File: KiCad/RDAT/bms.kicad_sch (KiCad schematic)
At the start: 0 parts

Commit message: kiCad BMS sadness
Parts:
- added C15: C, symbol Device:C
- added C16, C17, C18, C19: 0.1uF, symbol Device:C
- added J4: Conn_01x05_MountingPin, symbol Connector_Generic_MountingPin:Conn_01x05_MountingPin
- added R10, R11, R7, R9: R_US, symbol Device:R_US
- added U3: BQ40Z50RSMR-R2, RSM32_1P5X1P5_TEX, symbol BQ40Z50-R2:BQ40Z50RSMR-R2
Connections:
- new net: J4.4 (Pin_4), R9.1
- new net: C16.2, C17.1, R9.2, U3.3 (VC3)
- new net: J4.2 (Pin_2), R11.1
- new net: J4.3 (Pin_3), R10.1
- new net: J4.5 (Pin_5), R7.1
- new net: C17.2, C18.1, R10.2, U3.4 (VC2)
- new net: C15.2, U3.1 (PBI)
- new net: C16.1, R7.2, U3.2 (VC4)
- new net: C18.2, C19.1, R11.2, U3.5 (VC1)
- new net GND: C15.1, C19.2

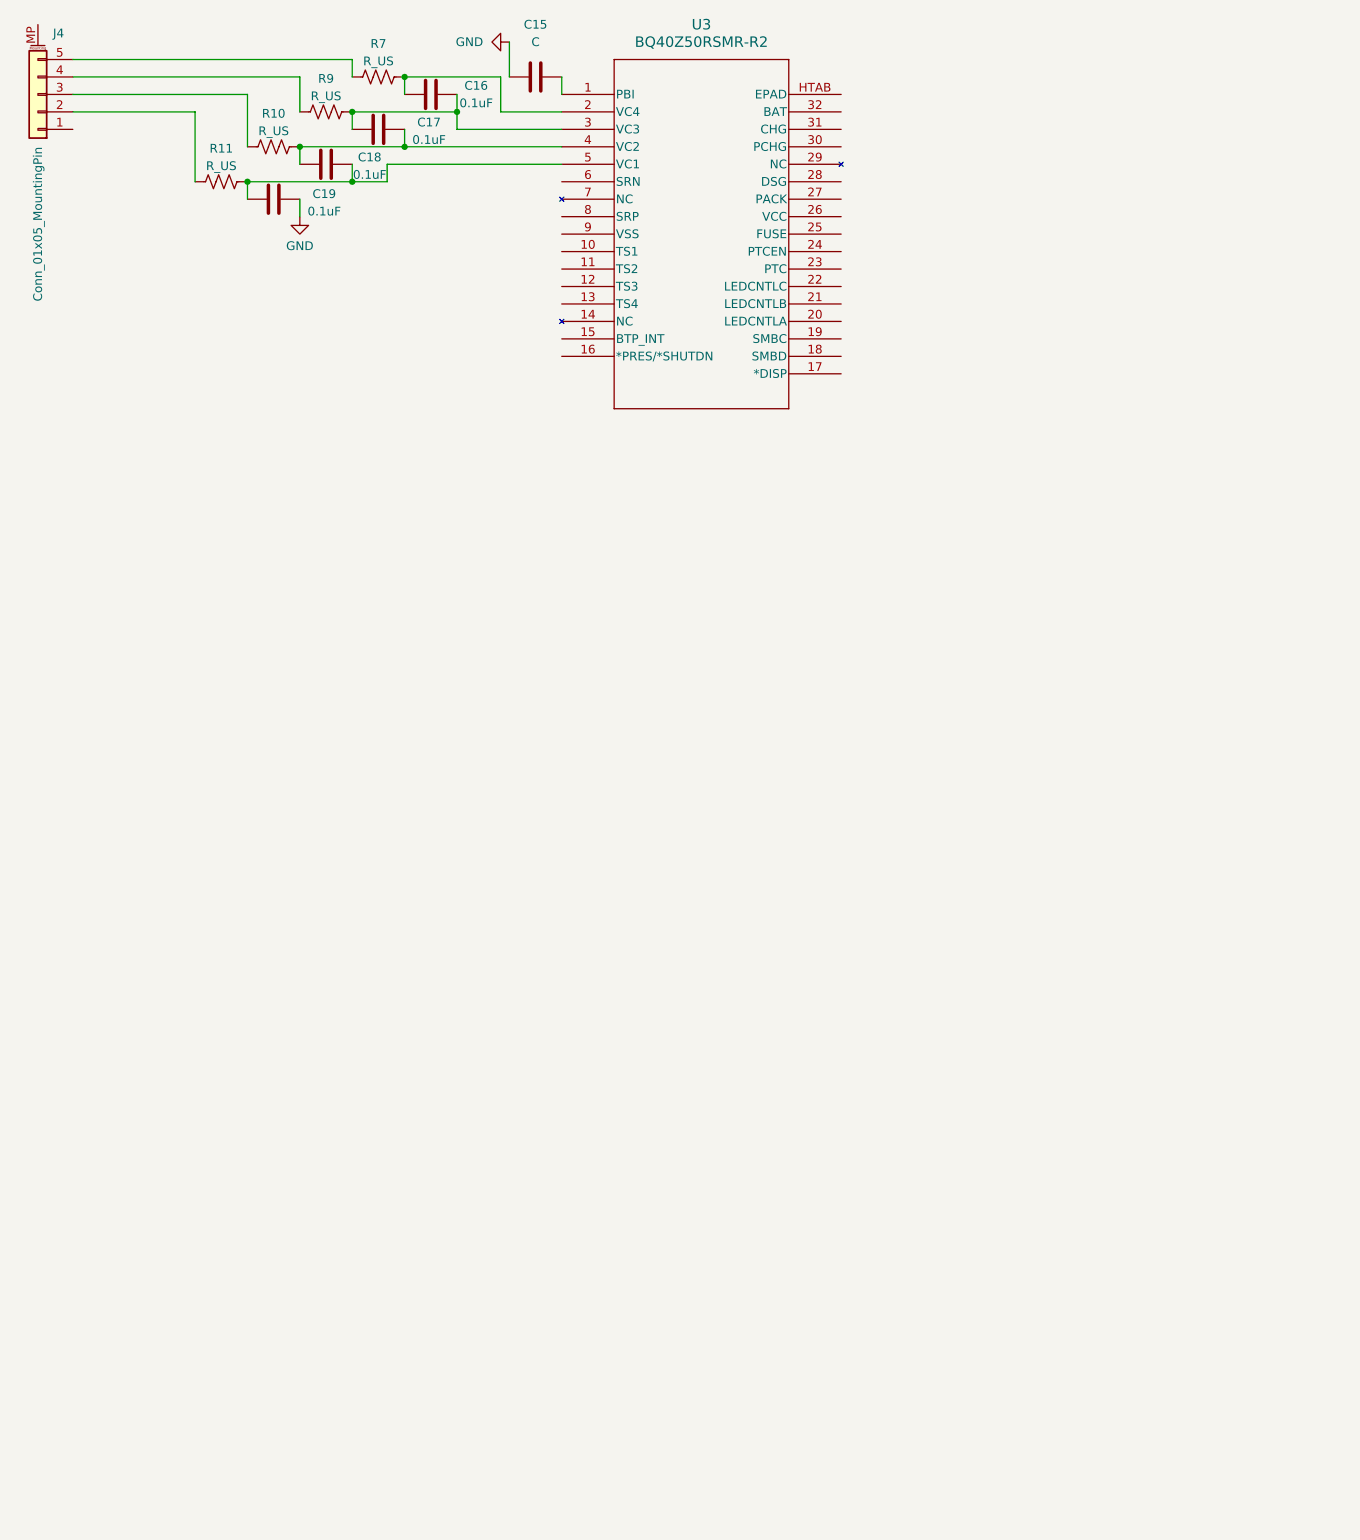
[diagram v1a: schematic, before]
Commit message: BMS circuitry
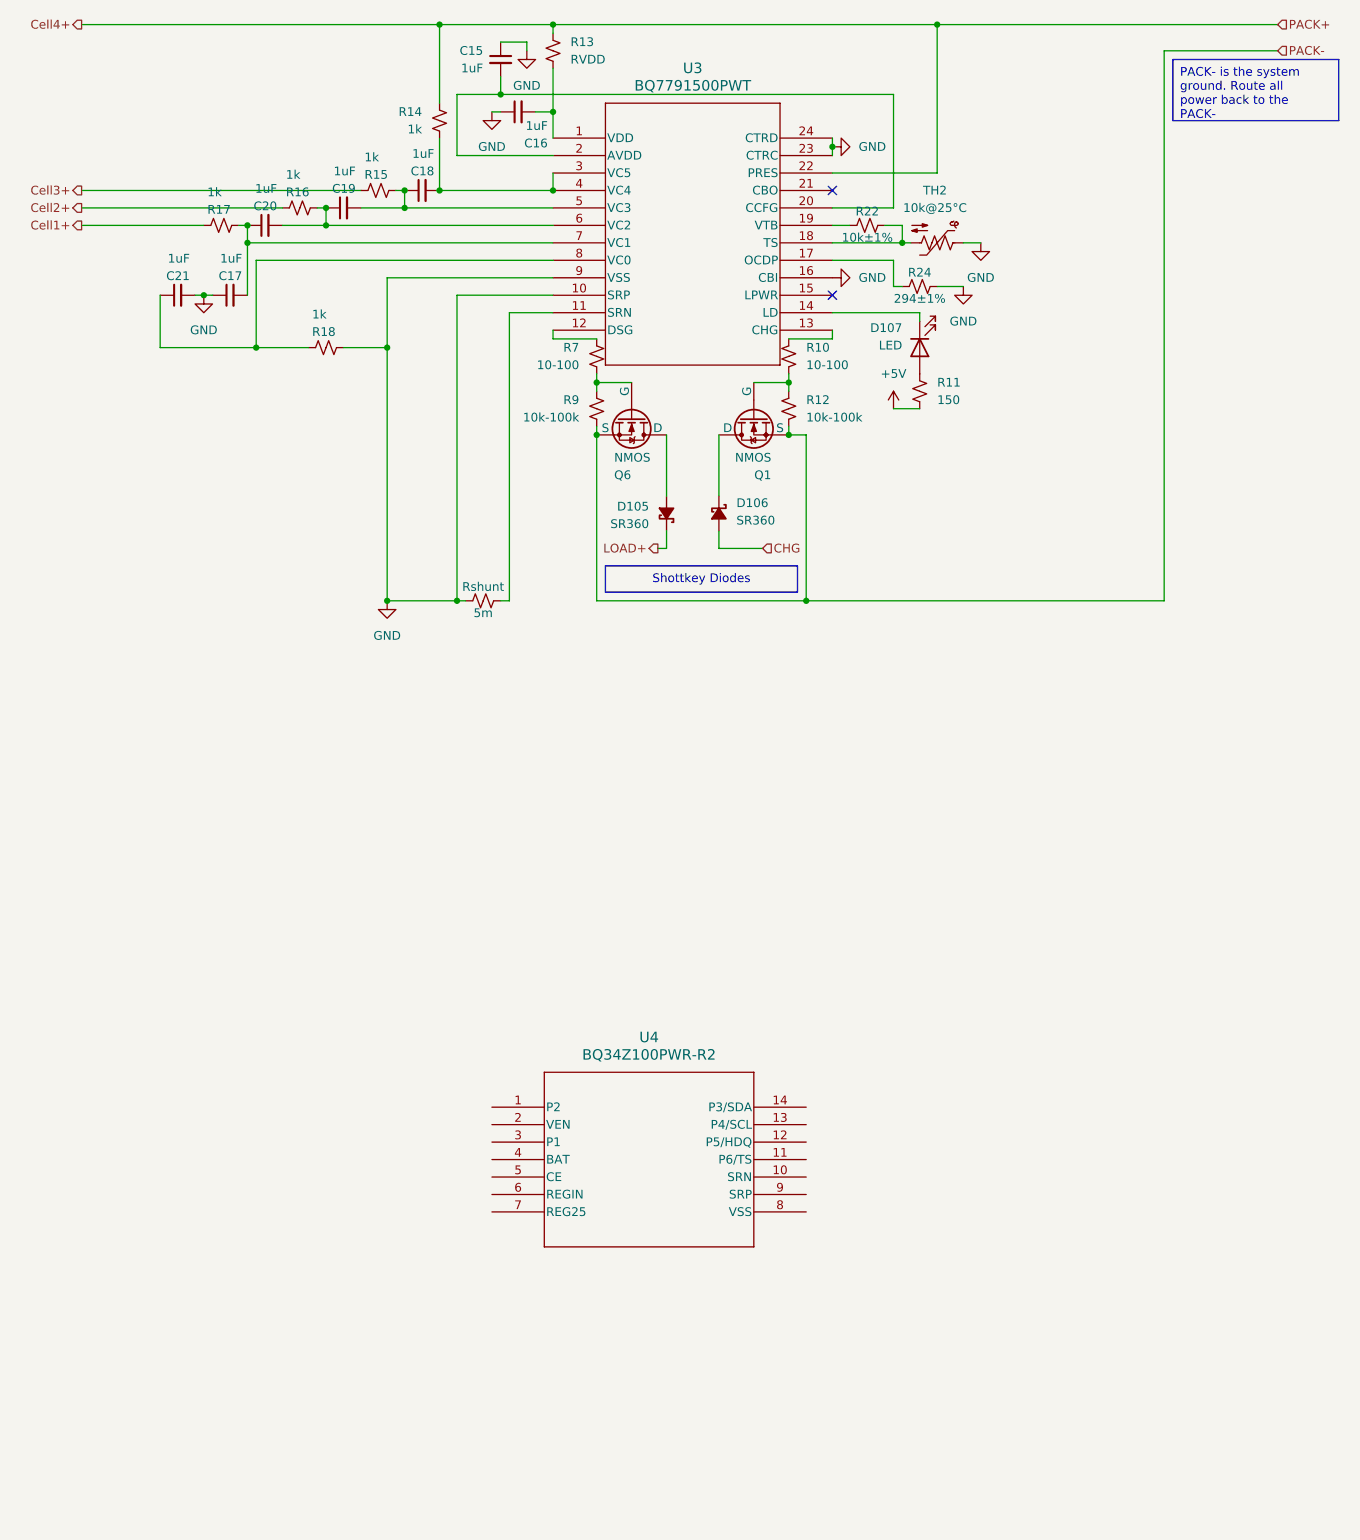
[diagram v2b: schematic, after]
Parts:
- removed C15: C, symbol Device:C
- removed C16, C17, C18, C19: 0.1uF, symbol Device:C
- removed J4: Conn_01x05_MountingPin, symbol Connector_Generic_MountingPin:Conn_01x05_MountingPin
- removed R10, R11, R7, R9: R_US, symbol Device:R_US
- removed U3: BQ40Z50RSMR-R2, RSM32_1P5X1P5_TEX, symbol BQ40Z50-R2:BQ40Z50RSMR-R2
- added C15, C16, C17, C18, C19, C20, C21: 1uF, symbol Device:C_Small
- added D105, D106: SR360, symbol Device:D_Schottky_Small_Filled
- added D107: LED, symbol Device:LED
- added Q1, Q6: NMOS, symbol Simulation_SPICE:NMOS
- added R10, R7: 10-100, symbol Device:R_Small_US
- added R11: 150, symbol Device:R_Small_US
- added R12, R9: 10k-100k, symbol Device:R_Small_US
- added R13: RVDD, symbol Device:R_Small_US
- added R14, R15, R16, R17, R18: 1k, symbol Device:R_Small_US
- added R22: 10k±1%, symbol Device:R_Small_US
- added R24: 294±1%, symbol Device:R_Small_US
- added Rshunt: 5m, symbol Device:R_Small_US
- added TH2: 10k@25°C, symbol Device:Thermistor_NTC_US
- added U3: BQ7791500PWT, PW24_TEX, symbol BQ77915:BQ7791500PWT
- added U4: BQ34Z100PWR-R2, PW14_TEX, symbol BQ34Z100:BQ34Z100PWR-R2
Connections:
- net GND: now also C15.1, C16.1, C17.1, C21.2, R18.2, R24.2, Rshunt.1, TH2.1, U3.10 (SRP), U3.16 (CBI), U3.23 (CTRC), U3.24 (CTRD), U3.9 (VSS)
- new net: D106.1 (K), Q1.1 (D)
- new net: Q1.2 (G), R10.2, R12.1
- new net: R22.1, U3.19 (VTB)
- new net: R22.2, TH2.2, U3.18 (TS)
- new net: C21.1, R18.1, U3.8 (VC0)
- new net: C19.1, C20.2, R16.2, U3.6 (VC2)
- new net: Q6.2 (G), R7.2, R9.1
- new net: C17.2, C20.1, R17.2, U3.7 (VC1)
- new net: Rshunt.2, U3.11 (SRN)
- new net: R7.1, U3.12 (DSG)
- new net: C18.1, C19.2, R15.2, U3.5 (VC3)
- new net: C16.2, R13.2, U3.1 (VDD)
- new net: R10.1, U3.13 (CHG)
- new net: D105.2 (A), Q6.1 (D)
- new net: C18.2, R14.2, U3.3 (VC5), U3.4 (VC4)
- new net: D107.2 (A), R11.1
- new net: R24.1, U3.17 (OCDP)
- new net: D107.1 (K), U3.14 (LD)
- new net: C15.2, U3.2 (AVDD), U3.20 (CCFG)
- new net +5V: R11.2
- new net CHG: D106.2 (A)
- new net Cell1+: R17.1
- new net Cell2+: R16.1
- new net Cell3+: R15.1
- new net Cell4+: R13.1, R14.1, U3.22 (PRES)
- new net LOAD+: D105.1 (K)
- new net PACK-: Q1.3 (S), Q6.3 (S), R12.2, R9.2
- no-connect marks 0 -> 2

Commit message: Update BMS
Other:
- moved on the sheet: U4
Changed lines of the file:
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@@
 		)
 	)
-	(text_box "Shottkey Diodes\n"
-		(exclude_from_sim no)
-		(at 96.52 92.71 0)
-		(size 27.94 3.81)
+	(text_box "Not Strictly Nessessary"
+		(exclude_from_sim no)
+		(at 13.97 134.62 0)
+		(size 186.69 97.79)
+		(stroke
+			(width 0)
+			(type default)
+		)
+		(fill
+			(type none)
+		)
+		(effects
+			(font
+				(size 1.27 1.27)
+			)
+			(justify left top)
+		)
+	)
+	(text_box "Shottkey Diodes\n\nEnsure the MOSFETS:\n-have Rds(on) < 10m ohms\n-fully turn on and off in expected range\n"
+		(exclude_from_sim no)
+		(at 96.52 93.98 0)
+		(size 27.94 16.51)
 		(stroke
 			(width 0)
@@
 	(symbol
 		(lib_id "BQ34Z100:BQ34Z100PWR-R2")
-		(at 80.01 171.45 0)
+		(at 88.9 175.26 0)
 		(unit 1)
 		(exclude_from_sim no)
@@
 		(fields_autoplaced yes)
 		(property "Reference" "U4"
-			(at 102.87 161.29 0)
+			(at 111.76 165.1 0)
 			(effects
 				(font
@@
 		)
 		(property "Value" "BQ34Z100PWR-R2"
-			(at 102.87 163.83 0)
+			(at 111.76 167.64 0)
 			(effects
 				(font
@@
 		)
 		(property "Footprint" "PW14_TEX"
-			(at 80.01 171.45 0)
+			(at 88.9 175.26 0)
 			(effects
 				(font
@@
 		)
 		(property "Datasheet" "BQ34Z100PWR-R2"
-			(at 80.01 171.45 0)
+			(at 88.9 175.26 0)
 			(effects
 				(font
@@
 		)
 		(property "Description" ""
-			(at 80.01 171.45 0)
+			(at 88.9 175.26 0)
 			(effects
 				(font
@@
 			)
 		)
-		(property "Description" "Light emitting diode"
+		(property "Description" "Light emitting diode (CONSIDER MAKING LOW POWER)"
 			(at 142.24 60.96 0)
 			(effects
